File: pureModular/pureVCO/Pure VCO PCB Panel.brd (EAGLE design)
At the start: 70.8 x 128.4 mm, 0 parts

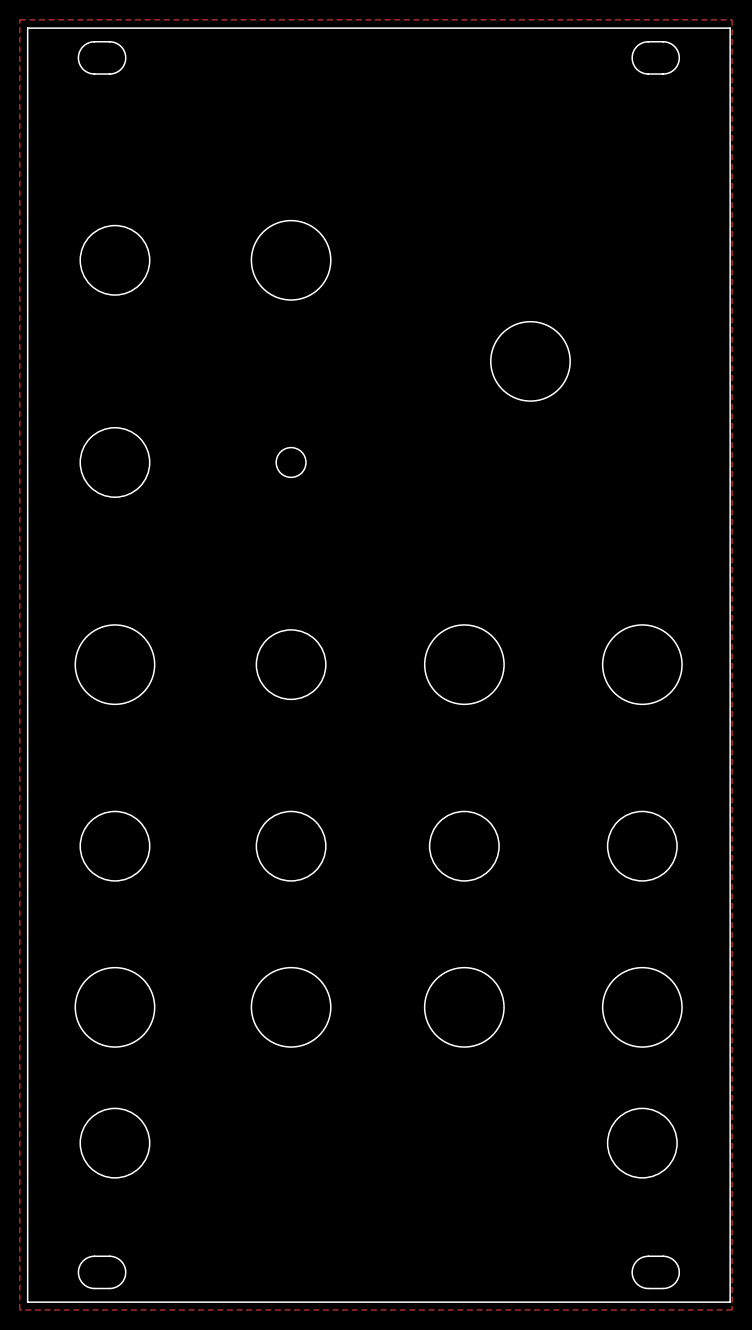
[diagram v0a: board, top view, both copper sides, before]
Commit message: VCO Updated to V3
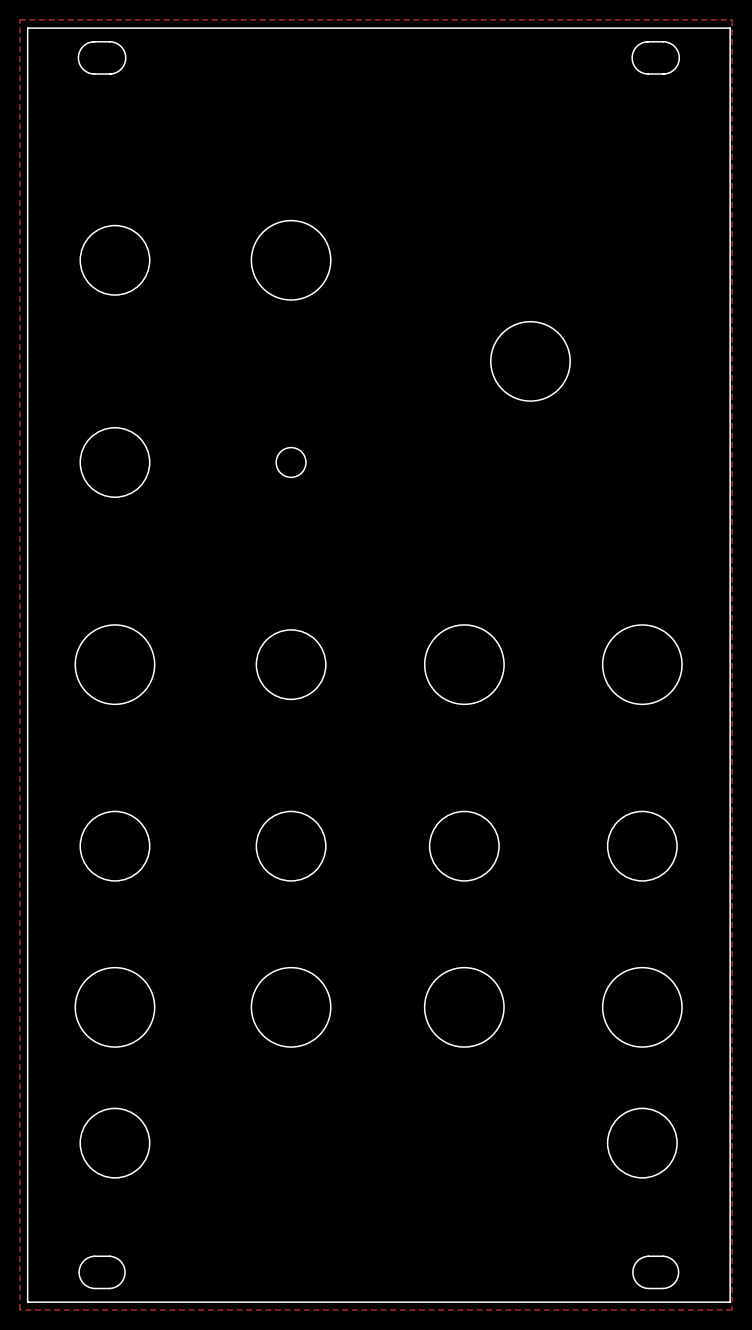
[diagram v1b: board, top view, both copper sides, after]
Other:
- outline, holes or cut-outs redrawn
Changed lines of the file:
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@@
 <?xml version="1.0" encoding="utf-8"?>
 <!DOCTYPE eagle SYSTEM "eagle.dtd">
-<eagle version="9.2.2">
+<eagle version="9.6.2">
 <drawing>
 <settings>
-<setting alwaysvectorfont="yes"/>
+<setting alwaysvectorfont="no"/>
 <setting verticaltext="up"/>
 </settings>
@@
 </layers>
 <board>
+<fusionsync huburn="a.cGVyc29uYWw6dWUyOGU4NzFl" projecturn="a.cGVyc29uYWw6dWUyOGU4NzFlIzIwMTcwMzA5NjY2OTYzMjY" f3durn="urn:adsk.wipprod:dm.lineage:cgysAq8KT0qWjdb3K4R4Hg" pcbguid="" lastpulledtime="2021-04-08T19:23:22Z" lastsyncedchangeguid="" latestrevisionid="130856a4-cbe4-4573-b86d-299ce434872c" lastsyncedrevisionid="130856a4-cbe4-4573-b86d-299ce434872c" lastboardhashguid="1ab80834-274e-3eee-c63d-ca0c87459a54" lastpushedtime="2021-04-09T13:27:13Z" linktopcb3d="true"/>
 <plain>
-<wire x1="0" y1="0" x2="0" y2="128.4" width="0.1524" layer="20"/>
-<wire x1="0" y1="128.4" x2="70.8" y2="128.4" width="0.1524" layer="20"/>
-<wire x1="70.8" y1="128.4" x2="70.8" y2="0" width="0.1524" layer="20"/>
-<wire x1="70.8" y1="0" x2="0" y2="0" width="0.1524" layer="20"/>
-<wire x1="6.74" y1="127.025" x2="8.26" y2="127.025" width="0.1524" layer="20"/>
-<wire x1="6.74" y1="123.775" x2="8.26" y2="123.775" width="0.1524" layer="20"/>
-<wire x1="8.26" y1="127.025" x2="8.26" y2="123.775" width="0.1524" layer="20" curve="-180"/>
-<wire x1="6.74" y1="127.025" x2="6.74" y2="123.775" width="0.1524" layer="20" curve="180"/>
-<wire x1="6.74" y1="4.625" x2="8.26" y2="4.625" width="0.1524" layer="20"/>
-<wire x1="6.74" y1="1.375" x2="8.26" y2="1.375" width="0.1524" layer="20"/>
-<wire x1="6.74" y1="4.625" x2="6.74" y2="1.375" width="0.1524" layer="20" curve="180"/>
-<wire x1="8.26" y1="4.625" x2="8.26" y2="1.375" width="0.1524" layer="20" curve="-180"/>
-<wire x1="62.55" y1="127.025" x2="64.05" y2="127.025" width="0.1524" layer="20"/>
-<wire x1="64.05" y1="123.775" x2="62.55" y2="123.775" width="0.1524" layer="20"/>
-<wire x1="64.05" y1="127.025" x2="64.05" y2="123.775" width="0.1524" layer="20" curve="-180"/>
-<wire x1="62.55" y1="123.775" x2="62.55" y2="127.025" width="0.1524" layer="20" curve="-180"/>
-<wire x1="62.55" y1="4.625" x2="64.05" y2="4.625" width="0.1524" layer="20"/>
-<wire x1="62.55" y1="1.375" x2="64.05" y2="1.375" width="0.1524" layer="20"/>
-<wire x1="64.05" y1="4.625" x2="64.05" y2="1.375" width="0.1524" layer="20" curve="-180"/>
-<wire x1="62.55" y1="1.375" x2="62.55" y2="4.625" width="0.1524" layer="20" curve="-180"/>
-<circle x="8.8" y="29.712" radius="4" width="0.1524" layer="20"/>
-<circle x="8.8" y="45.952" radius="3.5" width="0.1524" layer="20"/>
-<circle x="8.8" y="64.25" radius="4" width="0.1524" layer="20"/>
-<circle x="8.8" y="84.625" radius="3.5" width="0.1524" layer="20"/>
-<circle x="26.55" y="84.625" radius="1.5" width="0.1524" layer="20"/>
-<circle x="26.55" y="64.25" radius="3.5" width="0.1524" layer="20"/>
-<circle x="26.55" y="45.952" radius="3.5" width="0.1524" layer="20"/>
-<circle x="26.55" y="29.712" radius="4" width="0.1524" layer="20"/>
-<circle x="8.8" y="105" radius="3.5" width="0.1524" layer="20"/>
-<circle x="26.55" y="105" radius="4" width="0.1524" layer="20"/>
-<circle x="8.8" y="16.025" radius="3.5" width="0.1524" layer="20"/>
-<circle x="44.01" y="29.712" radius="4" width="0.1524" layer="20"/>
-<circle x="44.01" y="45.952" radius="3.5" width="0.1524" layer="20"/>
-<circle x="44.015" y="64.25" radius="4" width="0.1524" layer="20"/>
-<circle x="50.675" y="94.813" radius="4" width="0.1524" layer="20"/>
-<circle x="61.95" y="64.25" radius="4" width="0.1524" layer="20"/>
-<circle x="61.95" y="45.952" radius="3.5" width="0.1524" layer="20"/>
-<circle x="61.95" y="29.712" radius="4" width="0.1524" layer="20"/>
-<circle x="61.95" y="16.025" radius="3.5" width="0.1524" layer="20"/>
 <rectangle x1="27.9273" y1="6.6675" x2="30.7213" y2="6.6929" layer="29"/>
 <rectangle x1="31.1785" y1="6.6675" x2="32.3469" y2="6.6929" layer="29"/>
@@
 <rectangle x1="42.9895" y1="122.1105" x2="45.9613" y2="122.1359" layer="29"/>
 <rectangle x1="47.6631" y1="122.1105" x2="50.6095" y2="122.1359" layer="29"/>
+<circle x="61.95" y="16.025" radius="3.5" width="0.1524" layer="20"/>
+<circle x="61.95" y="29.712" radius="4" width="0.1524" layer="20"/>
+<circle x="61.95" y="45.952" radius="3.5" width="0.1524" layer="20"/>
+<circle x="61.95" y="64.25" radius="4" width="0.1524" layer="20"/>
+<circle x="50.675" y="94.813" radius="4" width="0.1524" layer="20"/>
+<circle x="44.015" y="64.25" radius="4" width="0.1524" layer="20"/>
+<circle x="44.01" y="45.952" radius="3.5" width="0.1524" layer="20"/>
+<circle x="44.01" y="29.712" radius="4" width="0.1524" layer="20"/>
+<circle x="8.8" y="16.025" radius="3.5" width="0.1524" layer="20"/>
+<circle x="26.55" y="105" radius="4" width="0.1524" layer="20"/>
+<circle x="8.8" y="105" radius="3.5" width="0.1524" layer="20"/>
+<circle x="26.55" y="29.712" radius="4" width="0.1524" layer="20"/>
+<circle x="26.55" y="45.952" radius="3.5" width="0.1524" layer="20"/>
+<circle x="26.55" y="84.625" radius="1.5" width="0.1524" layer="20"/>
+<circle x="8.8" y="84.625" radius="3.5" width="0.1524" layer="20"/>
+<circle x="8.8" y="64.25" radius="4" width="0.1524" layer="20"/>
+<circle x="8.8" y="45.952" radius="3.5" width="0.1524" layer="20"/>
+<circle x="8.8" y="29.712" radius="4" width="0.1524" layer="20"/>
+<wire x1="6.5984" y1="127.019" x2="6.74" y2="123.775" width="0.1524" layer="20" curve="175"/>
+<wire x1="6.5984" y1="127.019" x2="6.74" y2="127.025" width="0.1524" layer="20"/>
+<wire x1="6.74" y1="127.025" x2="8.26" y2="127.025" width="0.1524" layer="20"/>
+<wire x1="8.4016" y1="123.781" x2="8.26" y2="127.025" width="0.1524" layer="20" curve="175"/>
+<wire x1="8.4016" y1="123.781" x2="8.26" y2="123.775" width="0.1524" layer="20"/>
+<wire x1="8.26" y1="123.775" x2="6.74" y2="123.775" width="0.1524" layer="20"/>
+<wire x1="6.74" y1="4.625" x2="6.74" y2="1.375" width="0.1524" layer="20" curve="175"/>
+<wire x1="6.74" y1="4.625" x2="8.26" y2="4.625" width="0.1524" layer="20"/>
+<wire x1="8.26" y1="1.375" x2="8.26" y2="4.625" width="0.1524" layer="20" curve="175"/>
+<wire x1="8.26" y1="1.375" x2="6.74" y2="1.375" width="0.1524" layer="20"/>
+<wire x1="62.4084" y1="127.019" x2="62.55" y2="123.775" width="0.1524" layer="20" curve="175"/>
+<wire x1="62.4084" y1="127.019" x2="62.55" y2="127.025" width="0.1524" layer="20"/>
+<wire x1="62.55" y1="127.025" x2="64.05" y2="127.025" width="0.1524" layer="20"/>
+<wire x1="64.1916" y1="123.781" x2="64.05" y2="127.025" width="0.1524" layer="20" curve="175"/>
+<wire x1="64.1916" y1="123.781" x2="64.05" y2="123.775" width="0.1524" layer="20"/>
+<wire x1="64.05" y1="123.775" x2="62.55" y2="123.775" width="0.1524" layer="20"/>
+<wire x1="62.55" y1="4.625" x2="62.55" y2="1.375" width="0.1524" layer="20" curve="175"/>
+<wire x1="62.55" y1="4.625" x2="64.05" y2="4.625" width="0.1524" layer="20"/>
+<wire x1="64.05" y1="1.375" x2="64.05" y2="4.625" width="0.1524" layer="20" curve="175"/>
+<wire x1="64.05" y1="1.375" x2="62.55" y2="1.375" width="0.1524" layer="20"/>
+<circle x="26.55" y="64.25" radius="3.5" width="0.1524" layer="20"/>
+<wire x1="0" y1="128.4" x2="0" y2="0" width="0.1524" layer="20"/>
+<wire x1="0" y1="0" x2="70.8" y2="0" width="0.1524" layer="20"/>
+<wire x1="70.8" y1="0" x2="70.8" y2="128.4" width="0.1524" layer="20"/>
+<wire x1="70.8" y1="128.4" x2="0" y2="128.4" width="0.1524" layer="20"/>
 </plain>
 <attributes>
@@
 </signals>
 <mfgpreviewcolors>
-<mfgpreviewcolor name="soldermaskcolor" color="0xC8008000"/>
+<mfgpreviewcolor name="soldermaskcolor" color="0xC8000000"/>
 <mfgpreviewcolor name="silkscreencolor" color="0xFFFEFEFE"/>
 <mfgpreviewcolor name="backgroundcolor" color="0xFF282828"/>
-<mfgpreviewcolor name="coppercolor" color="0xFFFFBF00"/>
+<mfgpreviewcolor name="coppercolor" color="0xFFD1D1D1"/>
 <mfgpreviewcolor name="substratecolor" color="0xFF786E46"/>
 </mfgpreviewcolors>
 </board>
 </drawing>
+<compatibility>
+<note version="8.3" severity="warning">
+Since Version 8.3, EAGLE supports Fusion synchronisation.
+This feature will not be available in this version and saving
+the document will break the link to the Fusion PCB feature.
+</note>
+</compatibility>
 </eagle>
